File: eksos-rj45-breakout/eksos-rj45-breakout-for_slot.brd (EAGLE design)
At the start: 264.5 x 70 mm, 7 parts, among them X1 RJ45-8X-DS1130, X2 RJ45-8X-DS1130

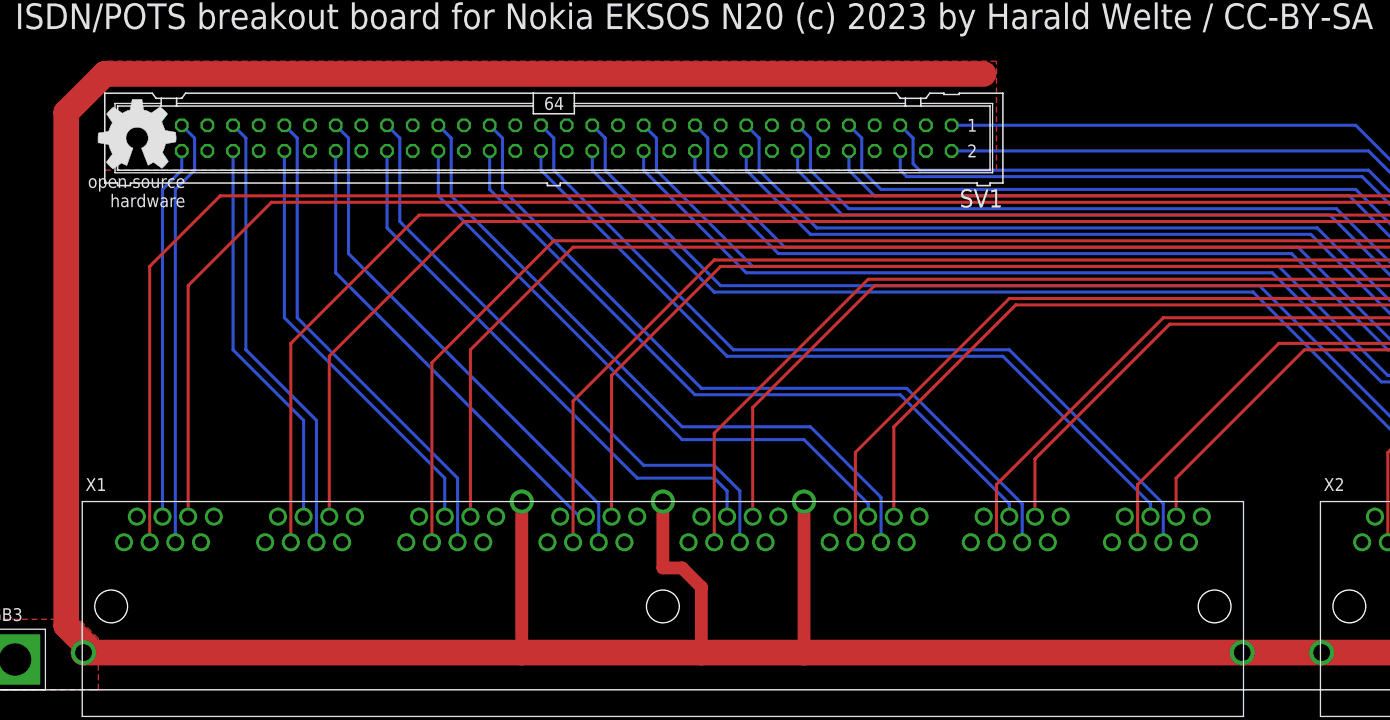
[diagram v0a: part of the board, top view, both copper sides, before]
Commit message: eksos-rj45-breakout: Move OSHW logo to have no overlap
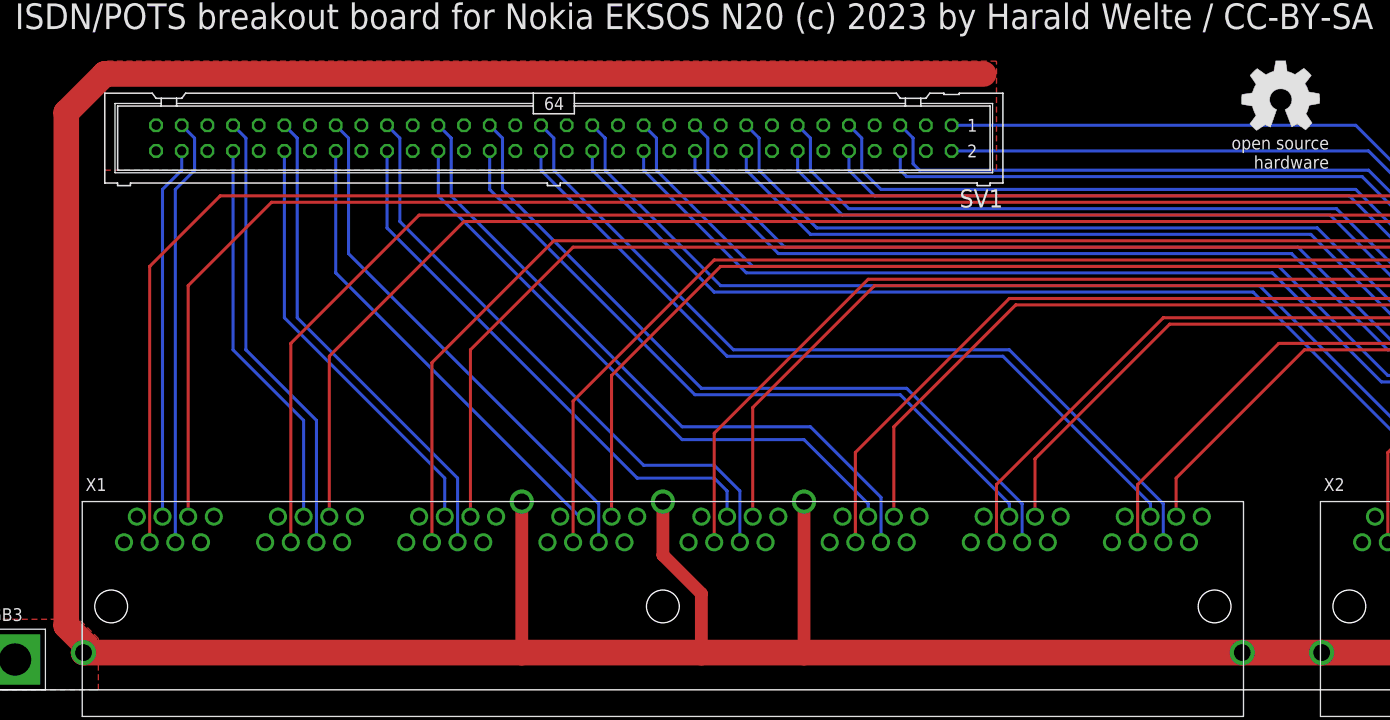
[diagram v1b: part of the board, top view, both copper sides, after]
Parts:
- moved U$1 113.3 mm to (132.2, 58.4)
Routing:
- net SHLD: track 626.0 -> 624.9 mm
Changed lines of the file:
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@@
 <element name="GB3" library="mechanical" package="GB6X6X12_VIA" value="GEWINDEBLOCK-6X6X12M3" x="7" y="3"/>
 <element name="GB4" library="mechanical" package="GB6X6X12_VIA" value="GEWINDEBLOCK-6X6X12M3" x="257.5" y="3"/>
-<element name="U$1" library="oshw" package="OSHW_8MM" value="" x="19.05" y="54.61"/>
+<element name="U$1" library="oshw" package="OSHW_8MM" value="" x="132.25" y="58.42"/>
 </elements>
 <signals>
@@
 <wire x1="57.15" y1="18.635" x2="57.15" y2="3.685" width="1.27" layer="1"/>
 <wire x1="85.09" y1="18.635" x2="85.09" y2="3.685" width="1.27" layer="1"/>
-<wire x1="71.12" y1="18.635" x2="71.12" y2="12.065" width="1.27" layer="1"/>
-<wire x1="71.12" y1="12.065" x2="73.025" y2="12.065" width="1.27" layer="1"/>
-<wire x1="73.025" y1="12.065" x2="74.93" y2="10.16" width="1.27" layer="1"/>
-<wire x1="74.93" y1="10.16" x2="74.93" y2="3.685" width="1.27" layer="1"/>
+<wire x1="71.12" y1="18.635" x2="71.12" y2="13.335" width="1.27" layer="1"/>
+<wire x1="71.12" y1="13.335" x2="74.93" y2="9.525" width="1.27" layer="1"/>
+<wire x1="74.93" y1="9.525" x2="74.93" y2="3.685" width="1.27" layer="1"/>
 <wire x1="179.705" y1="18.635" x2="179.705" y2="3.685" width="1.27" layer="1"/>
 <wire x1="207.645" y1="18.635" x2="207.645" y2="3.685" width="1.27" layer="1"/>
